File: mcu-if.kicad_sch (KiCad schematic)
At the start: 52 parts, among them J501 MCU_USB, J502 SD_Card, J503 CONN_DISP, J504 RJ45_Amphenol_RJMG1BD3B8K1ANR, SW501 BTN0, SW502 BTN1, SW503 BTN2, SW504 BTN3, U501 KSZ8081RNA

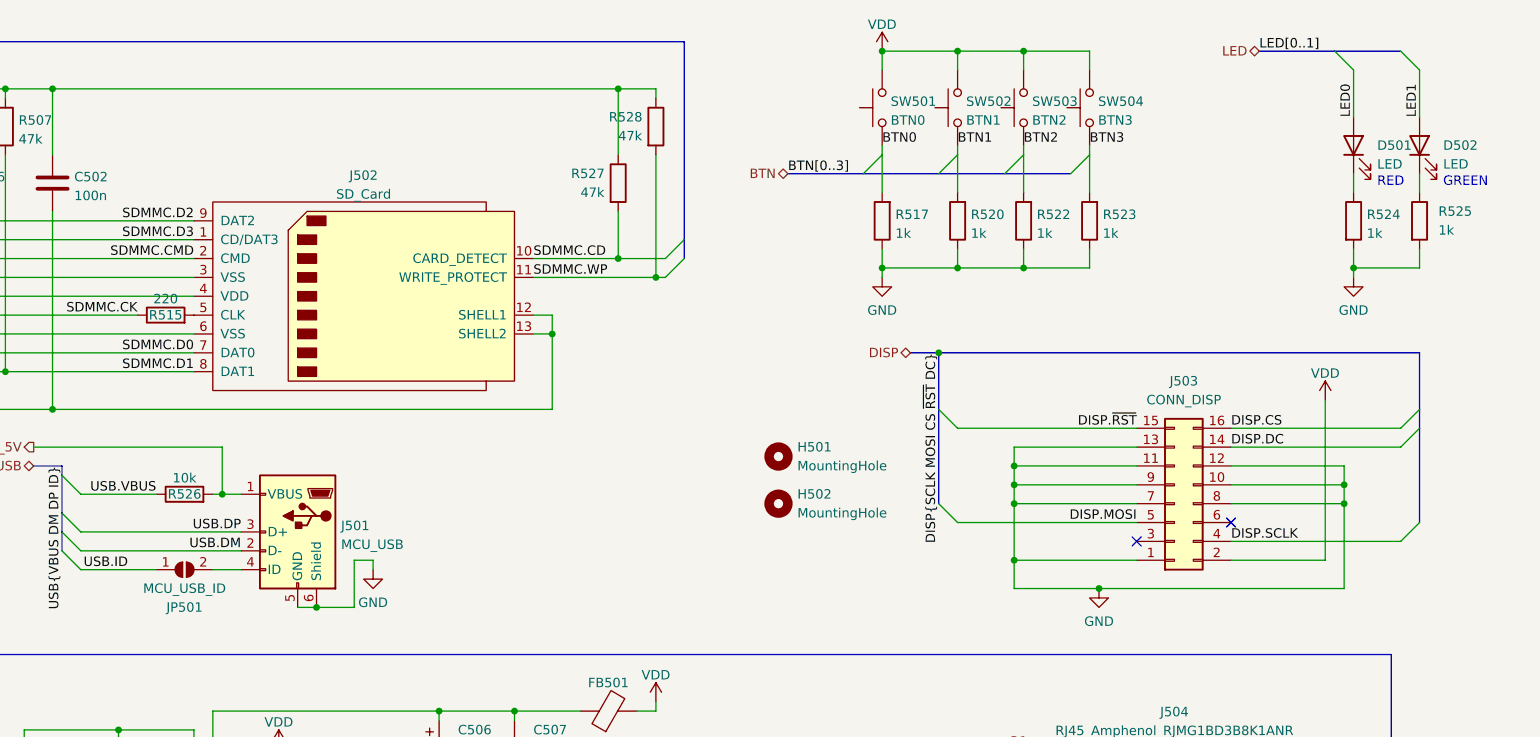
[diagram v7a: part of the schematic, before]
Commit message: Move labels on switches, jumpers and so on to a separate Label property from the Value property.
Value must be the same for components that are physically the same, otherwise it screws up the BOM. But that means we need to add each label manually.
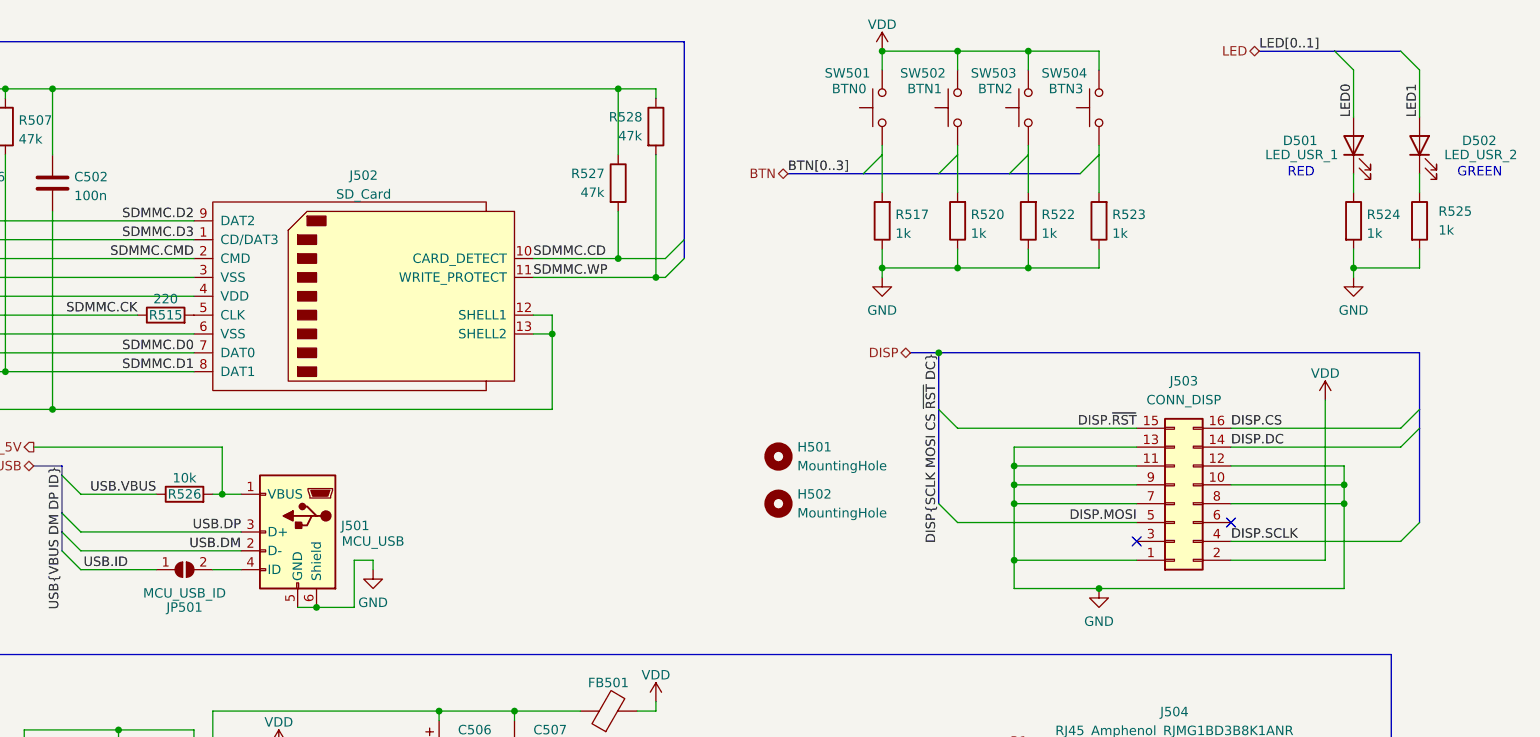
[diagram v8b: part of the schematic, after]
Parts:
- D501: Label (none) -> LED_USR_1
- D502: Label (none) -> LED_USR_2
- J501: value MCU_USB -> USB_Mini-B; Label (none) -> MCU_USB
- J503: value CONN_DISP -> PinSocket_2.54mm_2x08; Label (none) -> CONN_DISP
- JP501: value MCU_USB_ID -> Jumper; Label (none) -> MCU_USB_ID; now left out of the parts list
- SW501: value BTN0 -> DTSMW69N; Label (none) -> BTN0
- SW502: value BTN1 -> DTSMW69N; Label (none) -> BTN1
- SW503: value BTN2 -> DTSMW69N; Label (none) -> BTN2
- SW504: value BTN3 -> DTSMW69N; Label (none) -> BTN3
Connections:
- net BTN0: no longer names the net of R517.2, SW501.1
- net BTN1: no longer names the net of R520.2, SW502.1
- net BTN2: no longer names the net of R522.2, SW503.1
- net BTN3: no longer names the net of R523.2, SW504.1
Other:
- moved on the sheet: R522, R523, SW503, SW504
